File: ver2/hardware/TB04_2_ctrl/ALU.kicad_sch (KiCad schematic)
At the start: 8 parts, among them J801 Conn_02x05_Odd_Even, J802 Conn_02x05_Odd_Even, J803 Conn_02x05_Odd_Even, J804 Conn_02x05_Odd_Even, J805 Conn_02x05_Odd_Even, J806 Conn_02x05_Odd_Even, J807 Conn_02x05_Odd_Even, J808 Conn_02x05_Odd_Even

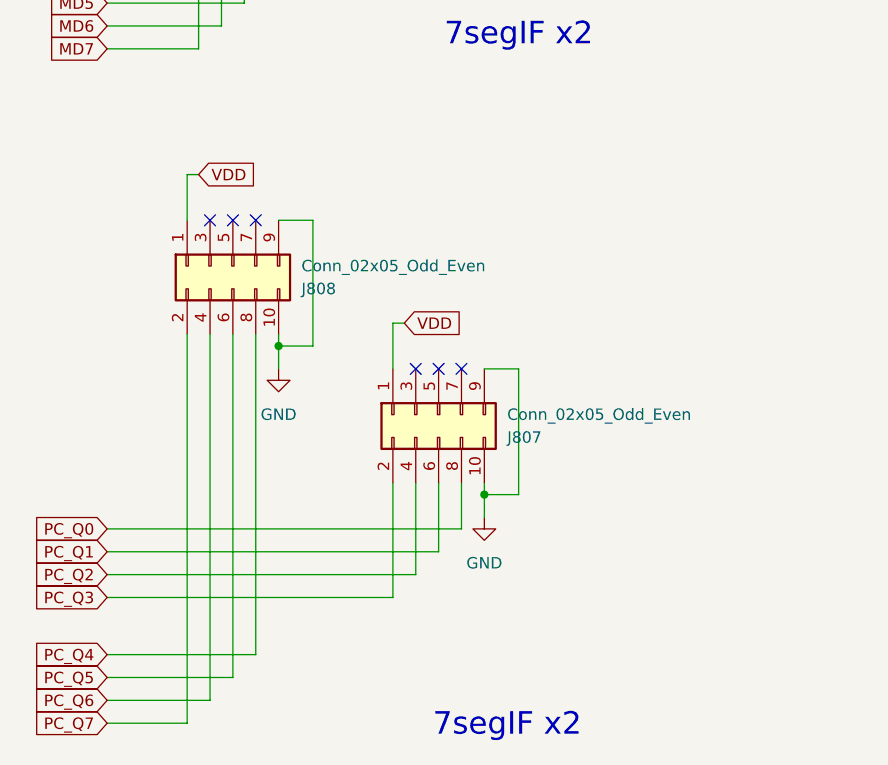
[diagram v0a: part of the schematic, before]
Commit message: ver2: 制御基板を分割完了・不要シートを整理(基板4分割の3枚目)
TB04_2_ctrl を分割完了。ai-reviewで検証し合格。
- 64信号すべてバスへ引き出し済み、ピン位置は確定表と完全一致
- 署名が変わったのは J101 のみ(USB-C→40ピンバスヘッダ)
- 電源入口は TB04_4_io のみ。他基板はバス1のVDD/GNDから受ける
- 各プロジェクトから未使用シートのファイルを削除

Co-Authored-By: Claude Opus 5 <noreply@anthropic.com>
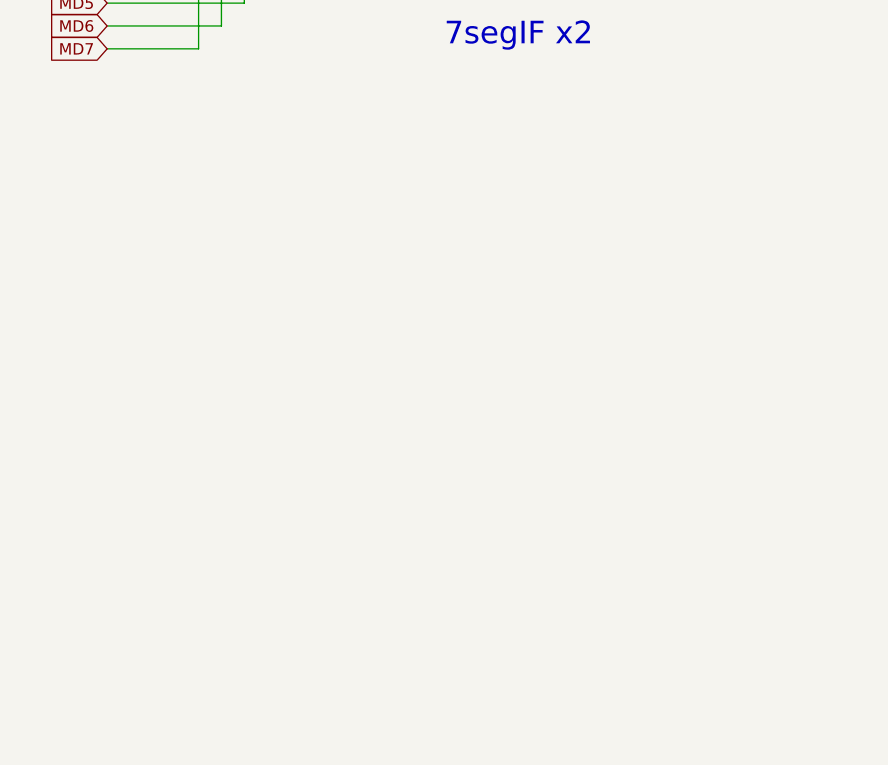
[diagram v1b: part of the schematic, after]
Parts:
- removed J807, J808: Conn_02x05_Odd_Even, symbol Connector_Generic:Conn_02x05_Odd_Even
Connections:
- no-connect marks 24 -> 18
